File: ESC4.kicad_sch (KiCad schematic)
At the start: 35 parts, among them J13 MOTOR_A, J14 MOTOR_B, J15 MOTOR_C, Q20 Q_NMOS_GDS, Q21 Q_NMOS_GDS, Q22 Q_NMOS_GDS, Q23 Q_NMOS_GDS, Q24 Q_NMOS_GDS, Q25 Q_NMOS_GDS, U20 STM32G071GBUxN, U21 DRV8300D

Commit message: Footprints and revision
Added the missing footprints.
Updated a all the schematics.
Completed an initial review of the schematics.

TODO:
Perform a deep review of the schematics before committing to layout.
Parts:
- removed Q20, Q21, Q22, Q23, Q24, Q25: Q_NMOS_GDS, symbol Transistor_FET:Q_NMOS_GDS
- added Q12, Q13, Q14: XRS306D, Custom_Parts:PDFN8, symbol Transistor_FET:Q_Dual_NMOS_S1G1S2G2D2D1
- C81: renamed from C70; footprint (none) -> Capacitor_SMD:C_0603_1608Metric
- C82: renamed from C71; footprint (none) -> Capacitor_SMD:C_0603_1608Metric
- C83: renamed from C72; footprint (none) -> Capacitor_SMD:C_0805_2012Metric
- C84: renamed from C73; footprint (none) -> Capacitor_SMD:C_0603_1608Metric
- C85: renamed from C74; footprint (none) -> Capacitor_SMD:C_0603_1608Metric
- C86: renamed from C75; footprint (none) -> Capacitor_SMD:C_0603_1608Metric
- R76: renamed from R69; footprint (none) -> Resistor_SMD:R_0603_1608Metric
- R77: renamed from R70; footprint (none) -> Resistor_SMD:R_0603_1608Metric
- R78: renamed from R71; footprint (none) -> Resistor_SMD:R_0603_1608Metric
- R79: renamed from R72; footprint (none) -> Resistor_SMD:R_0603_1608Metric
- R80: renamed from R73; footprint (none) -> Resistor_SMD:R_0603_1608Metric
- R81: renamed from R74; footprint (none) -> Resistor_SMD:R_0603_1608Metric
- R82: renamed from R75; footprint (none) -> Resistor_SMD:R_0603_1608Metric
- R83: renamed from R76; footprint (none) -> Resistor_SMD:R_0603_1608Metric
- R84: renamed from R77; footprint (none) -> Resistor_SMD:R_0603_1608Metric
- R85: renamed from R78; footprint (none) -> Resistor_SMD:R_0603_1608Metric
- R86: renamed from R79; footprint (none) -> Resistor_SMD:R_0603_1608Metric
- R87: renamed from R80; footprint (none) -> Resistor_SMD:R_0603_1608Metric
- R88: renamed from R81; footprint (none) -> Resistor_SMD:R_0603_1608Metric
- R89: renamed from R82; footprint (none) -> Resistor_SMD:R_0603_1608Metric
- R90: renamed from R83; footprint (none) -> Resistor_SMD:R_0603_1608Metric
- R91: renamed from R84; footprint (none) -> Resistor_SMD:R_0603_1608Metric
- renumbered J13 to J14, J14 to J15, J15 to J16, TP18 to TP17, TP19 to TP18, U20 to U21, U21 to U22
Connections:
- net GND: now also Q12.3 (S), Q13.3 (S), Q14.3 (S)
- net MOTOR_A: now also Q12.1 (S), Q12.5 (D)
- net MOTOR_B: now also Q13.1 (S), Q13.5 (D)
- net MOTOR_C: now also Q14.1 (S), Q14.5 (D)
- net VBAT: now also Q12.6 (D), Q13.6 (D), Q14.6 (D)
- net at R90.2: now also Q14.2 (G)
- net at R89.2: now also Q13.4 (G)
- net at R88.2: now also Q13.2 (G)
- net at R91.2: now also Q14.4 (G)
- net at R86.2: now also Q12.2 (G)
- net at R87.2: now also Q12.4 (G)

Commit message: ESC design
Updated the ESC schematics.
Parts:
- renumbered C81 to C48, C82 to C49, C83 to C50, C84 to C51, C85 to C52, C86 to C53, J14 to J12, J15 to J13, J16 to J14, Q12 to Q11, Q13 to Q12, Q14 to Q13, R76 to R68, R77 to R69, R78 to R70, R79 to R71, R80 to R72, R81 to R73, R82 to R74, R83 to R75, R84 to R76, R85 to R77, R86 to R78, R87 to R79, R88 to R80, R89 to R81, R90 to R82, R91 to R83, U21 to U13, U22 to U14
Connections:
- net BSTA: now reaches C51.1, U14.20 (BSTA)
- net GLB_IN: now reaches Q12.4 (G), R81.2
- net GHB_IN: now reaches Q12.2 (G), R80.2
- net GHC_IN: now reaches Q13.2 (G), R82.2
- net BSTC: now reaches C53.1, U14.14 (BSTC)
- net BSTB: now reaches C52.1, U14.17 (BSTB)
- net GLC_IN: now reaches Q13.4 (G), R83.2
- net ESC: now reaches R71.1, U13.12 (PA6)
- net GHA_IN: now reaches Q11.2 (G), R78.2
- net GLA_IN: now reaches Q11.4 (G), R79.2
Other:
- company: (none) -> DavidMolTor
- title: (none) -> THUNDER HORSE
- moved on the sheet: J12, J13, J14, Q11A, Q11B, Q12A, Q12B, Q13A, Q13B

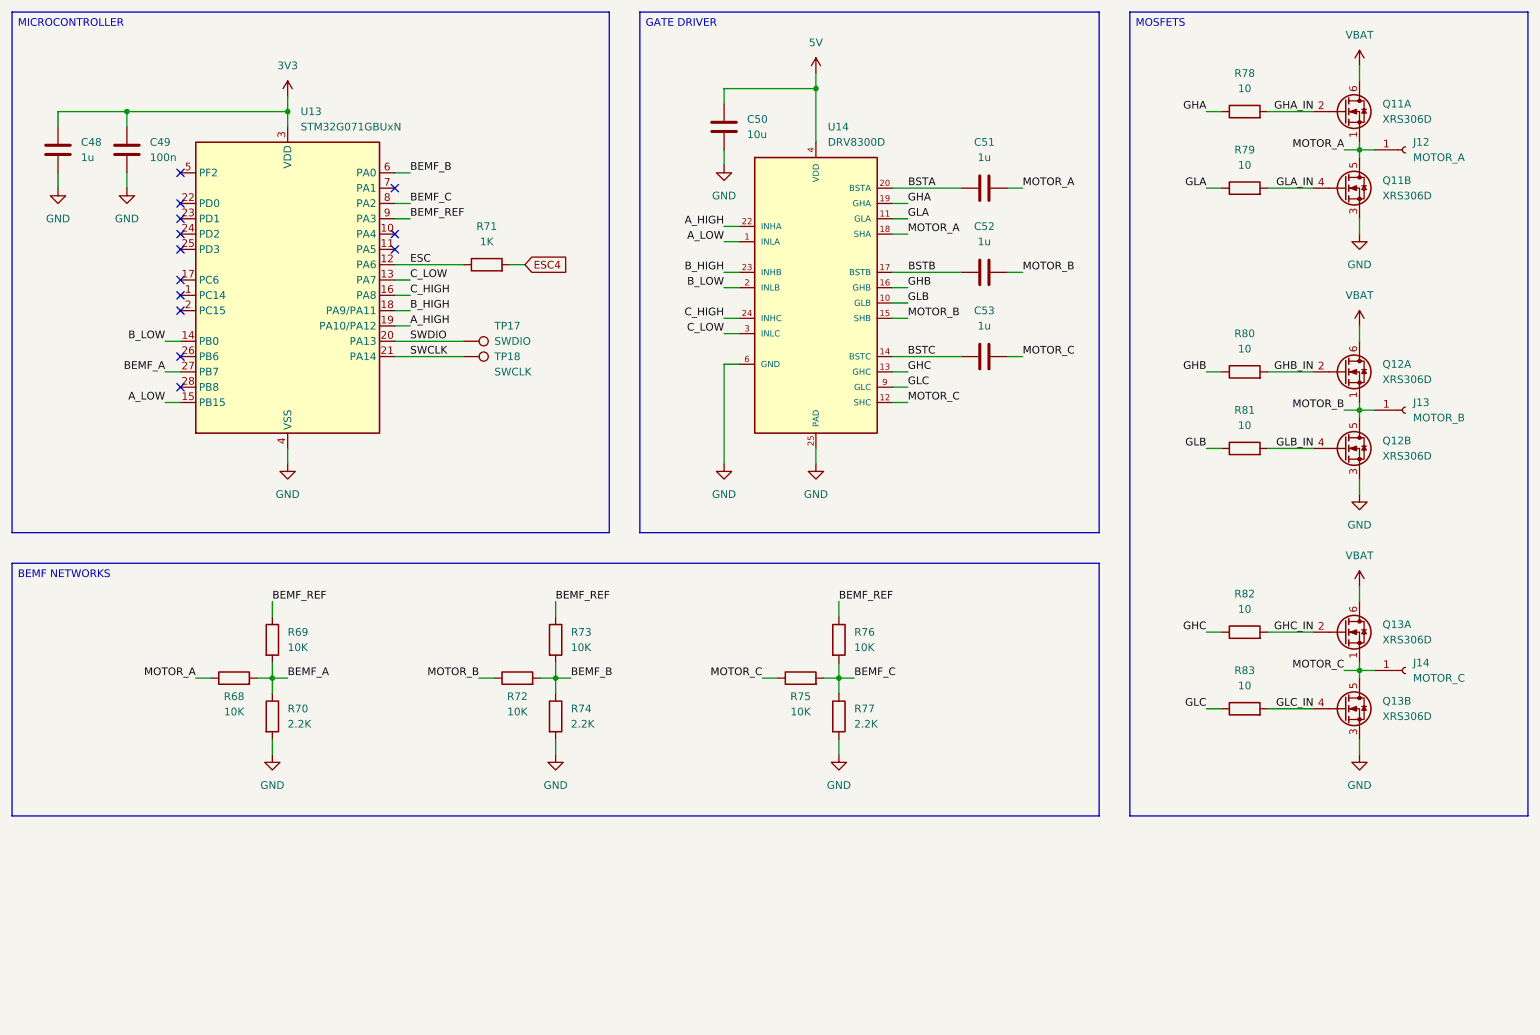
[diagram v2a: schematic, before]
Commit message: Connectors and tag
Added bulk capacitance for each ESC.
Added SWD connector.
Updated all tags.

TODO:
Add pads for the unconnected GPIO pins.
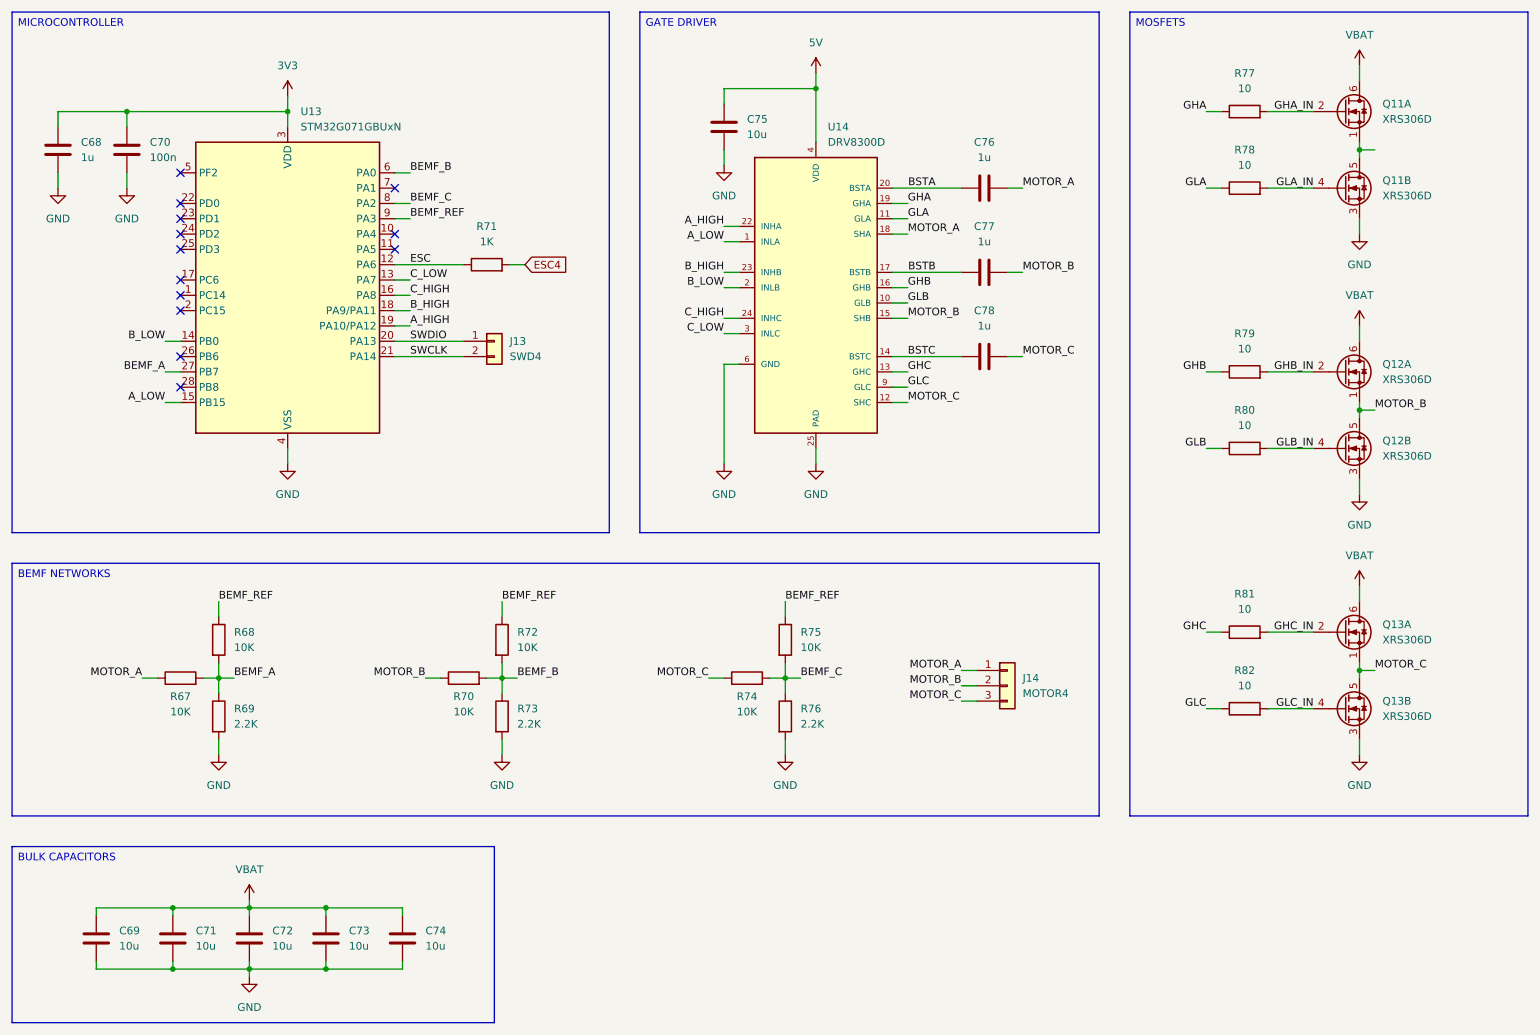
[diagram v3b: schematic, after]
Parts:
- removed J12: MOTOR_A, TestPoint:TestPoint_Pad_D2.0mm, symbol Connector:Conn_01x01_Socket
- removed J13: MOTOR_B, TestPoint:TestPoint_Pad_D2.0mm, symbol Connector:Conn_01x01_Socket
- removed J14: MOTOR_C, TestPoint:TestPoint_Pad_D2.0mm, symbol Connector:Conn_01x01_Socket
- removed R83: 10, Resistor_SMD:R_0603_1608Metric, symbol Device:R
- removed TP17: SWDIO, TestPoint:TestPoint_Pad_D1.0mm, symbol Connector:TestPoint
- removed TP18: SWCLK, TestPoint:TestPoint_Pad_D1.0mm, symbol Connector:TestPoint
- added C69, C71, C72, C73, C74: 10u, symbol Device:C
- added J13: SWD4, symbol Connector_Generic:Conn_01x02
- added J14: MOTOR4, Custom_Parts:PAD_3_SQUARE_SOLID_2.0x2.0mm_P2.5mm, symbol Connector_Generic:Conn_01x03
- added R67: 10K, Resistor_SMD:R_0603_1608Metric, symbol Device:R
- R69, R73, R76: value 10K -> 2.2K
- R70, R74: value 2.2K -> 10K
- R77: value 2.2K -> 10
- renumbered C48 to C68, C49 to C70, C50 to C75, C51 to C76, C52 to C77, C53 to C78
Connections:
- net BEMF_A: now also R69.1, R67.2; no longer R69.2, R70.1
- net BEMF_B: now also R70.2, R73.1; no longer R73.2, R74.1
- net BEMF_C: now also R74.2, R76.1; no longer R76.2, R77.1
- net BEMF_REF: now also R68.1, R72.1, R75.1; no longer R69.1, R73.1, R76.1
- net GHA: now also R77.1; no longer R78.1
- net GHA_IN: now also R77.2; no longer R78.2
- net GHB: now also R79.1; no longer R80.1
- net GHB_IN: now also R79.2; no longer R80.2
- net GHC: now also R81.1; no longer R82.1
- net GHC_IN: now also R81.2; no longer R82.2
- net GLA: now also R78.1; no longer R79.1
- net GLA_IN: now also R78.2; no longer R79.2
- net GLB: now also R80.1; no longer R81.1
- net GLB_IN: now also R80.2; no longer R81.2
- net GLC: now also R82.1
- net GLC_IN: now also R82.2
- net GND: now also R69.2, R73.2, R76.2, C69.2, C71.2, C72.2, C73.2, C74.2; no longer R70.2, R74.2, R77.2
- net MOTOR_A: now also J14.1 (Pin_1), R67.1; no longer Q11.1 (S), Q11.5 (D), R68.1
- net MOTOR_B: now also R70.1, J14.2 (Pin_2); no longer R72.1
- net MOTOR_C: now also R74.1, J14.3 (Pin_3); no longer R75.1
- net SWCLK: now also J13.2 (Pin_2)
- net SWDIO: now also J13.1 (Pin_1)
- net VBAT: now also C69.1, C71.1, C72.1, C73.1, C74.1
- new net: Q11.1 (S), Q11.5 (D)

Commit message: Missing labels and revision
First complete revision of the schematic.
Added missing labels.

TODO:
Continue reviewing the schematic.
Include net coloring.
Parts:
- C69, C71, C72, C73, C74: footprint (none) -> Capacitor_SMD:C_1206_3216Metric
- J13: footprint (none) -> Custom_Parts:PAD_2_SQUARE_SOLID_1.0x1.0mm_P1.5mm
- Q11, Q12, Q13: footprint Custom_Parts:PDFN8 -> Custom_Parts:PDFN8_DUAL_3.3x3.3mm
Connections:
- net MOTOR_A: now also Q11.1 (S), Q11.5 (D)
- no-connect marks 13 -> 15
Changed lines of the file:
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@@
 	)
 	(no_connect
+		(at 143.51 83.82)
+	)
+	(no_connect
 		(at 50.8 85.09)
 	)
@@
 	)
 	(no_connect
+		(at 143.51 81.28)
+	)
+	(no_connect
 		(at 86.36 59.69)
 	)
@@
 	(wire
 		(pts
+			(xy 143.51 88.9) (xy 140.97 88.9)
+		)
+		(stroke
+			(width 0)
+			(type default)
+		)
+	)
+	(wire
+		(pts
 			(xy 30.48 39.37) (xy 30.48 41.91)
 		)
@@
 	(wire
 		(pts
-			(xy 143.51 81.28) (xy 140.97 81.28)
+			(xy 140.97 73.66) (xy 143.51 73.66)
 		)
 		(stroke
@@
 	(wire
 		(pts
-			(xy 140.97 73.66) (xy 143.51 73.66)
+			(xy 220.98 125.73) (xy 223.52 125.73)
 		)
 		(stroke
@@
 	(wire
 		(pts
-			(xy 220.98 125.73) (xy 223.52 125.73)
+			(xy 104.14 133.35) (xy 104.14 135.89)
 		)
 		(stroke
@@
 	(wire
 		(pts
-			(xy 104.14 133.35) (xy 104.14 135.89)
+			(xy 36.83 181.61) (xy 49.53 181.61)
 		)
 		(stroke
@@
 	(wire
 		(pts
-			(xy 36.83 181.61) (xy 49.53 181.61)
+			(xy 151.13 133.35) (xy 151.13 135.89)
 		)
 		(stroke
@@
 	(wire
 		(pts
-			(xy 151.13 133.35) (xy 151.13 135.89)
+			(xy 140.97 60.96) (xy 143.51 60.96)
 		)
 		(stroke
@@
 	(wire
 		(pts
-			(xy 140.97 60.96) (xy 143.51 60.96)
+			(xy 57.15 130.81) (xy 57.15 133.35)
 		)
 		(stroke
@@
 	(wire
 		(pts
-			(xy 57.15 130.81) (xy 57.15 133.35)
+			(xy 140.97 88.9) (xy 140.97 97.79)
 		)
 		(stroke
@@
 	(wire
 		(pts
-			(xy 140.97 81.28) (xy 140.97 97.79)
-		)
-		(stroke
-			(width 0)
-			(type default)
-		)
-	)
-	(wire
-		(pts
 			(xy 48.26 77.47) (xy 50.8 77.47)
 		)
@@
 		)
 	)
+	(label "MOTOR_A"
+		(at 248.92 45.72 0)
+		(effects
+			(font
+				(size 1.27 1.27)
+			)
+			(justify left bottom)
+		)
+	)
 	(label "B_HIGH"
 		(at 140.97 66.04 180)
@@
 			)
 		)
-		(property "Footprint" "Custom_Parts:PDFN8"
+		(property "Footprint" "Custom_Parts:PDFN8_DUAL_3.3x3.3mm"
 			(at 248.92 125.73 0)
 			(effects
@@
 	)
 	(symbol
-		(lib_id "power:GND")
-		(at 140.97 97.79 0)
-		(unit 1)
-		(exclude_from_sim no)
-		(in_bom yes)
-		(on_board yes)
-		(dnp no)
-		(fields_autoplaced yes)
-		(property "Reference" "#PWR0135"
-			(at 140.97 104.14 0)
-			(effects
-				(font
-					(size 1.27 1.27)
-				)
-				(hide yes)
-			)
-		)
-		(property "Value" "GND"
-			(at 140.97 102.87 0)
-			(effects
-				(font
-					(size 1.27 1.27)
-				)
-			)
-		)
-		(property "Footprint" ""
-			(at 140.97 97.79 0)
-			(effects
-				(font
-					(size 1.27 1.27)
-				)
-				(hide yes)
-			)
-		)
-		(property "Datasheet" ""
-			(at 140.97 97.79 0)
-			(effects
-				(font
-					(size 1.27 1.27)
-				)
-				(hide yes)
-			)
-		)
-		(property "Description" "Power symbol creates a global label with name \"GND\" , ground"
-			(at 140.97 97.79 0)
-			(effects
-				(font
-					(size 1.27 1.27)
-				)
-				(hide yes)
-			)
-		)
-		(pin "1"
-		)
-		(instances
-			(project "ThunderHorse"
-				(path "/ac187c6c-fa53-41cc-bce1-6f39a42a92e8/807a5f6f-4255-4cf0-8d90-acd62bb18590/c0aa3042-c8c9-4ed2-b5c5-e577006d065c"
-					(reference "#PWR0135")
-					(unit 1)
-				)
-			)
-		)
-	)
-	(symbol
 		(lib_id "Device:R")
 		(at 57.15 139.7 0)
@@
 			)
 		)
-		(property "Footprint" ""
+		(property "Footprint" "Capacitor_SMD:C_1206_3216Metric"
 			(at 50.4952 180.34 0)
 			(effects
@@
 	)
 	(symbol
+		(lib_id "power:GND")
+		(at 140.97 97.79 0)
+		(unit 1)
+		(exclude_from_sim no)
+		(in_bom yes)
+		(on_board yes)
+		(dnp no)
+		(fields_autoplaced yes)
+		(property "Reference" "#PWR0135"
+			(at 140.97 104.14 0)
+			(effects
+				(font
+					(size 1.27 1.27)
+				)
+				(hide yes)
+			)
+		)
+		(property "Value" "GND"
+			(at 140.97 102.87 0)
+			(effects
+				(font
+					(size 1.27 1.27)
+				)
+			)
+		)
+		(property "Footprint" ""
+			(at 140.97 97.79 0)
+			(effects
+				(font
+					(size 1.27 1.27)
+				)
+				(hide yes)
+			)
+		)
+		(property "Datasheet" ""
+			(at 140.97 97.79 0)
+			(effects
+				(font
+					(size 1.27 1.27)
+				)
+				(hide yes)
+			)
+		)
+		(property "Description" "Power symbol creates a global label with name \"GND\" , ground"
+			(at 140.97 97.79 0)
+			(effects
+				(font
+					(size 1.27 1.27)
+				)
+				(hide yes)
+			)
+		)
+		(pin "1"
+		)
+		(instances
+			(project "ThunderHorse"
+				(path "/ac187c6c-fa53-41cc-bce1-6f39a42a92e8/807a5f6f-4255-4cf0-8d90-acd62bb18590/c0aa3042-c8c9-4ed2-b5c5-e577006d065c"
+					(reference "#PWR0135")
+					(unit 1)
+				)
+			)
+		)
+	)
+	(symbol
 		(lib_id "Device:C")
 		(at 87.63 176.53 0)
@@
 			)
 		)
-		(property "Footprint" ""
+		(property "Footprint" "Capacitor_SMD:C_1206_3216Metric"
 			(at 88.5952 180.34 0)
 			(effects
@@
 			)
 		)
-		(property "Footprint" "Custom_Parts:PDFN8"
+		(property "Footprint" "Custom_Parts:PDFN8_DUAL_3.3x3.3mm"
 			(at 248.92 138.43 0)
 			(effects
@@
 		(pin "4"
 		)
+		(pin "8"
+		)
+		(pin "7"
+		)
+		(pin "21"
+		)
+		(pin "5"
+		)
 		(instances
 			(project "ThunderHorse"
@@
 			)
 		)
-		(property "Footprint" "Custom_Parts:PDFN8"
+		(property "Footprint" "Custom_Parts:PDFN8_DUAL_3.3x3.3mm"
 			(at 248.92 39.37 0)
 			(effects
@@
 			)
 		)
-		(property "Footprint" ""
+		(property "Footprint" "Custom_Parts:PAD_2_SQUARE_SOLID_1.0x1.0mm_P1.5mm"
 			(at 102.87 77.47 0)
 			(effects
@@
 			)
 		)
-		(property "Footprint" "Custom_Parts:PDFN8"
+		(property "Footprint" "Custom_Parts:PDFN8_DUAL_3.3x3.3mm"
 			(at 248.92 95.25 0)
 			(effects
@@
 			)
 		)
-		(property "Footprint" "Custom_Parts:PDFN8"
+		(property "Footprint" "Custom_Parts:PDFN8_DUAL_3.3x3.3mm"
 			(at 248.92 52.07 0)
 			(effects
@@
 			)
 		)
-		(property "Footprint" ""
+		(property "Footprint" "Capacitor_SMD:C_1206_3216Metric"
 			(at 75.8952 180.34 0)
 			(effects
@@
 			)
 		)
-		(property "Footprint" "Custom_Parts:PDFN8"
+		(property "Footprint" "Custom_Parts:PDFN8_DUAL_3.3x3.3mm"
 			(at 248.92 82.55 0)
 			(effects
@@
 			)
 		)
-		(property "Footprint" ""
+		(property "Footprint" "Capacitor_SMD:C_1206_3216Metric"
 			(at 63.1952 180.34 0)
 			(effects
@@
 			)
 		)
-		(property "Footprint" ""
+		(property "Footprint" "Capacitor_SMD:C_1206_3216Metric"
 			(at 37.7952 180.34 0)
 			(effects

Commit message: ESC layout and footprints
Added the initial ESC layout.
Updated some footprints for compatibility.
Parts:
- removed C69, C71, C73: 10u, Capacitor_SMD:C_1206_3216Metric, symbol Device:C
- added C75, C76, C77, C78: 10u, Capacitor_SMD:C_1206_3216Metric, symbol Device:C
- J14: footprint Custom_Parts:PAD_3_SQUARE_SOLID_2.0x2.0mm_P2.5mm -> Custom_Parts:PAD_3_SQUARE_SOLID_2.5x2.5mm_P4.0mm
- renumbered C68 to C71, C70 to C73, C75 to C79, C76 to C80, C77 to C81, C78 to C82
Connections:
- net GND: now also C75.2, C76.2, C77.2, C78.2
- net VBAT: now also C75.1, C76.1, C77.1, C78.1

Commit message: Layout replication
Updated the ESC schematic to allow for layout replication.
Updated the PCB layout.
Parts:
- J13: value SWD4 -> SWD1
- J14: value MOTOR4 -> MOTOR1

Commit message: Initial layout
Completed an initial layout of the main components.

TODO
Route the ESCs and check the result.
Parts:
- renumbered C71 to C72, C72 to C73, C73 to C74, C74 to C75, C75 to C76, C76 to C77, C77 to C78, C78 to C79, C79 to C80, C80 to C81, C81 to C82, C82 to C83, Q11 to Q10, Q12 to Q11, Q13 to Q12, U13 to U14, U14 to U15

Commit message: Settings and ESC layout
Updated the PCB configuration options for manufacturing.
Completed the initial ESC layout.

TODO:
Replicate ESC layout.
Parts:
- J14: footprint Custom_Parts:PAD_3_SQUARE_SOLID_2.5x2.5mm_P4.0mm -> Custom_Parts:PAD_3_SQUARE_SOLID_2.5x2.5mm_P4.0mm_MOTOR
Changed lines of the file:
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@@
 			)
 		)
-		(property "Footprint" "Custom_Parts:PAD_3_SQUARE_SOLID_2.5x2.5mm_P4.0mm"
+		(property "Footprint" "Custom_Parts:PAD_3_SQUARE_SOLID_2.5x2.5mm_P4.0mm_MOTOR"
 			(at 187.96 134.62 0)
 			(effects
